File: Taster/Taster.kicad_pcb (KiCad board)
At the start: 2 copper layers, 30 x 30 mm, 55 parts, among them J1 I2C, J2 JTAG, J3 INTERFACE, M1 KNX_KLEMME, SW1 SW_Push, U1 EFM32PG12B500, U2 NCN5120, U3 MX25R8035F, Y1 32.768kHz, Y2 38.4MHz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

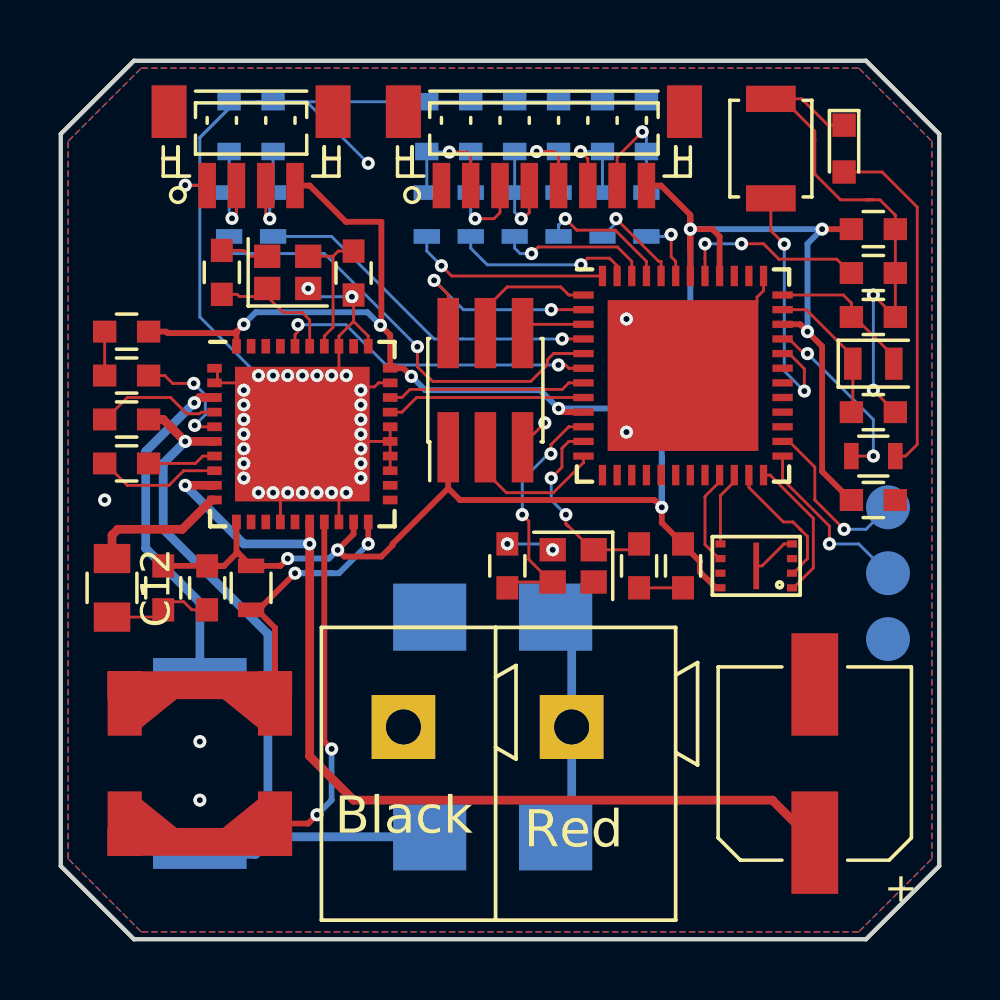
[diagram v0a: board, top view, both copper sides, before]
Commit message: Version 1.1.0 of the Taster board.
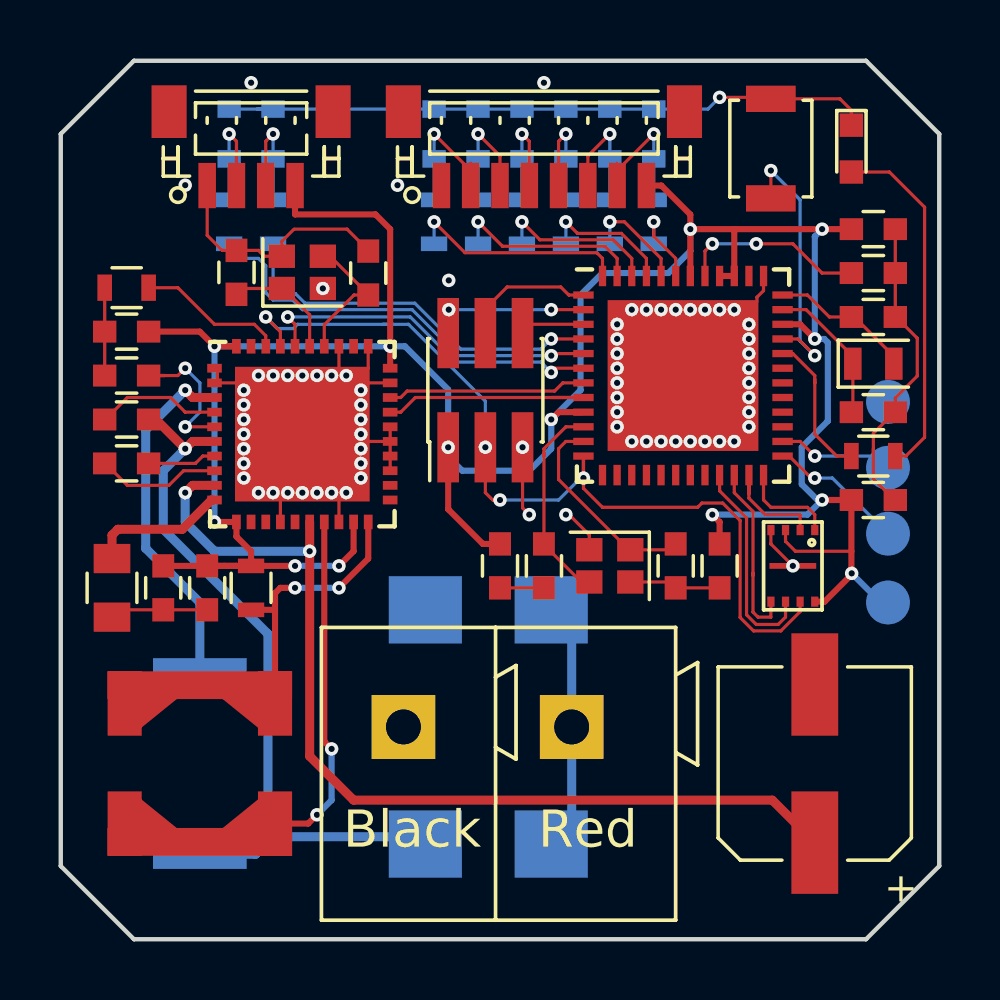
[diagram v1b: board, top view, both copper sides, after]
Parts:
- removed M1: KNX_KLEMME, KNXTransceiverBoard_V1.2:KNXTransceiverBoard_V1.2-KNX_KLEMME
- added C20: 100nF, Capacitors_SMD:C_0603, F.Cu at (85.0, 57.2)
- added J3: KNX_KLEMME, KNX:KNX_KLEMME, F.Cu at (84.2, 62.8)
- added R13: 0, Resistors_SMD:R_0603, F.Cu at (72.2, 47.8)
- added TP4: Test_Point, Measurement_Points:Measurement_Point_Round-SMD-Pad_Small, B.Cu at (98.2, 58.5)
- C14: value 4.7nF -> 220nF
- R2: value 22 -> 27
- SW1: value SW_Push -> PROG
- U2: value NCN5120 -> NCN5121
- moved TP1 5.85 mm to (98.2, 51.6)
- moved TP3 3.60 mm to (98.2, 56.1)
- moved TP2 1.35 mm to (98.2, 53.9)
- moved C10 1.25 mm to (92.5, 57.2)
- moved C4 1.25 mm to (91.0, 57.2)
- moved C5 1.25 mm to (86.5, 57.2), turned to 270 degrees
- moved U3 1.25 mm to (95.0, 57.2), turned to 270 degrees
- moved Y2 1.25 mm to (88.8, 57.2)
- moved C6 0.50 mm to (80.5, 47.2), turned to 90 degrees
- moved C7 0.50 mm to (76.0, 47.2)
- moved Y3 0.50 mm to (78.2, 47.2)
- moved D10 0.35 mm to (84.2, 42.5)
- moved D11 0.35 mm to (82.8, 42.5)
- moved D6 0.35 mm to (90.2, 42.5)
- moved D7 0.35 mm to (88.8, 42.5)
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- renumbered J3 to J2, J2 to J4
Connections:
- C10 pad 1: +3V3 -> 3V3-A
- C16 pad 1: +3V3 -> 3V3-A
- C17 pad 1: +3V3 -> 3V3-A
- C18 pad 1: +3V3 -> 3V3-A
- C8 pad 1: +3V3 -> 3V3-A
- C9 pad 1: +3V3 -> 3V3-A
- J1 pad 4: +3V3 -> 3V3-A
- J2 pad 8: +3V3 -> 3V3-A
- J4 pad 1: +3V3 -> 3V3-A
- R3 pad 1: +3V3 -> 3V3-A
- TP1 pad 1: Net-(TP1-Pad1) -> GND
- TP3 pad 1: GND -> Net-(TP3-Pad1)
- U1 pad 25: Net-(TP1-Pad1) -> Net-(TP3-Pad1)
- U1 pad 32: /SWITCH -> /LED
- U1 pad 33: /LED -> /SWITCH
- U1 pad 34: +3V3 -> 3V3-A
- U1 pad 39: Net-(U1-Pad39) -> 3V3-A
- U1 pad 40: +3V3 -> 3V3-A
- U1 pad 42: +3V3 -> 3V3-A
- U1 pad 9: +3V3 -> 3V3-A
- U2 pad 11: +3V3 -> 3V3-A
- U2 pad 19: +3V3 -> 3V3-A
- U2 pad 30: +3V3 -> 3V3-A
- U2 pad 37: /RESETB -> /RESET
- U2 pad 38: /FANIN -> Net-(R13-Pad2)
- U2 pad 40: +3V3 -> 3V3-A
- U3 pad 3: Net-(U3-Pad3) -> 3V3-A
- U3 pad 7: Net-(U3-Pad7) -> /RESET
- U3 pad 8: +3V3 -> 3V3-A
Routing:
- net 3V3-A: track 0.00 -> 99.1 mm, vias 0 -> 13
- net +3V3: track 93.5 -> 0.00 mm, vias 10 -> 0
- net /RESET: track 5.13 -> 31.9 mm, vias 0 -> 4
- net GND: track 122.4 -> 113.5 mm, vias 42 -> 71
- net Net-(TP1-Pad1): track 6.08 -> 0.00 mm, vias 1 -> 0
- net Net-(R13-Pad2): track 0.00 -> 5.04 mm
- net Net-(TP3-Pad1): track 0.00 -> 4.70 mm, vias 0 -> 1
- net /SCLK: track 3.31 -> 7.25 mm
- net /MOSI: track 2.55 -> 6.23 mm
- net /SWDIO: track 7.51 -> 4.60 mm
- net /SCL: track 16.3 -> 14.5 mm
- net /CS: track 5.02 -> 3.33 mm
- net Net-(TP2-Pad1): track 5.81 -> 4.20 mm
- net Net-(C5-Pad1): track 8.60 -> 7.17 mm, vias 2 -> 0
- net Net-(D11-Pad1): track 3.97 -> 5.31 mm
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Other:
- net class Default: clearance 0.1 -> 0.11; trace_width 0.1 -> 0.11; via_dia 0.45 -> 0.46; via_drill 0.2 -> 0.21
- net class Power: clearance 0.1 -> 0.11; trace_width 0.3 -> 0.31; via_dia 0.45 -> 0.46; via_drill 0.2 -> 0.21
- net class Power-3V3: clearance 0.1 -> 0.11; trace_width 0.2 -> 0.21; via_dia 0.45 -> 0.46; via_drill 0.2 -> 0.21
- rule trace_clearance: 0.1 -> 0.11
- board text added: "BasilFX 06 2018 V1.1.0"
- board text removed: "BasilFX 06/2018 V1.1.0"

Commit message: Version 1.2.0 of board
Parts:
- removed C20: 100nF, Capacitors_SMD:C_0603
- added C19: 100nF, Capacitor_SMD:C_0603_1608Metric, F.Cu at (85.0, 57.2)
- added R12: 0, Resistor_SMD:R_0603_1608Metric, F.Cu at (72.2, 46.5)
- C1, C10, C13, C14, C15, C16, C17, C18, C2, C3, C4, C5, C6, C7, C8, C9: footprint Capacitors_SMD:C_0603 -> Capacitor_SMD:C_0603_1608Metric
- C11: footprint Capacitors_SMD:CP_Elec_6.3x7.7 -> Capacitor_SMD:CP_Elec_6.3x7.7
- C12: footprint Capacitors_SMD:C_0805 -> Capacitor_SMD:C_0805_2012Metric
- D1: footprint LEDs:LED_0603 -> LED_SMD:LED_0603_1608Metric
- D10, D11, D4, D5, D6, D7, D8, D9: footprint Diodes_SMD:D_0603 -> Diode_SMD:D_0603_1608Metric
- D2, D3: footprint Diodes_SMD:D_SMB -> Diode_SMD:D_SMB
- J1: footprint Connectors_JST:JST_SH_BM04B-SRSS-TB_04x1.00mm_Straight -> Connector_JST:JST_SH_BM04B-SRSS-TB_1x04-1MP_P1.00mm_Vertical
- J2: footprint Connectors_JST:JST_SH_BM08B-SRSS-TB_08x1.00mm_Straight -> Connector_JST:JST_SH_BM08B-SRSS-TB_1x08-1MP_P1.00mm_Vertical
- J4: footprint Pin_Headers:Pin_Header_Straight_2x03_Pitch1.27mm_SMD -> Connector_PinHeader_1.27mm:PinHeader_2x03_P1.27mm_Vertical_SMD
- R1, R4, R5, R6, R7, R8, R9: value 220 -> 680; footprint Resistors_SMD:R_0603 -> Resistor_SMD:R_0603_1608Metric
- R10, R11: value 220 -> 0; footprint Resistors_SMD:R_0603 -> Resistor_SMD:R_0603_1608Metric
- R13: footprint Resistors_SMD:R_0603 -> Resistor_SMD:R_0603_1608Metric
- R2: footprint Resistors_SMD:R_2512 -> Resistor_SMD:R_2512_6332Metric
- R3: value R -> 1; footprint Resistors_SMD:R_0603 -> Resistor_SMD:R_0603_1608Metric
- SW1: footprint Buttons_Switches_SMD:SW_SPST_B3U-1000P -> Button_Switch_SMD:SW_SPST_B3U-1000P
- TP1, TP2, TP3, TP4: footprint Measurement_Points:Measurement_Point_Round-SMD-Pad_Small -> TestPoint:TestPoint_Pad_D1.0mm
- U1: footprint Housings_DFN_QFN:QFN-48-1EP_7x7mm_Pitch0.5mm -> Package_DFN_QFN:Infineon_MLPQ-48-1EP_7x7mm_P0.5mm_Pad5.15x5.15mm
- U2: footprint Housings_DFN_QFN:QFN-40-1EP_6x6mm_Pitch0.5mm -> Package_DFN_QFN:QFN-40-1EP_6x6mm_P0.5mm_EP4.6x4.6mm
- Y1: footprint Crystals:Crystal_SMD_2012-2pin_2.0x1.2mm -> Crystal:Crystal_SMD_2012-2Pin_2.0x1.2mm
- Y2: value 38.4MHz -> 40MHz; footprint Crystals:Crystal_SMD_2016-4pin_2.0x1.6mm -> Crystal:Crystal_SMD_2016-4Pin_2.0x1.6mm
- Y3: footprint Crystals:Crystal_SMD_2016-4pin_2.0x1.6mm -> Crystal:Crystal_SMD_2016-4Pin_2.0x1.6mm
- moved TP1 0.27 mm to (98.0, 51.8), turned to 0 degrees
- moved TP2 0.27 mm to (98.0, 54.0), turned to 0 degrees
- moved TP3 0.27 mm to (98.0, 56.2)
- moved C13 0.25 mm to (72.2, 51.0)
- moved C14 0.25 mm to (72.2, 54.0)
- moved C15 0.25 mm to (72.2, 52.5)
- moved C18 0.25 mm to (72.2, 49.5)
- moved R13 0.25 mm to (72.2, 48.0)
- moved TP4 0.25 mm to (98.0, 58.5)
- turned L1 to 90 degrees
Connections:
- U2 pad 37: /RESET -> Net-(R12-Pad2)
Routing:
- net GND: track 113.5 -> 137.9 mm
- net Net-(R12-Pad2): track 0.00 -> 6.69 mm, vias 0 -> 2
- net Net-(L1-Pad2): track 17.7 -> 11.4 mm
- net /RESET: track 31.9 -> 35.0 mm
- net Net-(C11-Pad1): track 33.2 -> 34.3 mm
- net /KNX+: track 26.9 -> 27.8 mm
- net Net-(C13-Pad1): track 5.32 -> 4.48 mm
- net Net-(R2-Pad2): track 12.1 -> 12.9 mm
- net Net-(D6-Pad1): track 5.29 -> 4.53 mm
- net Net-(D11-Pad1): track 5.31 -> 4.55 mm
- net 3V3-A: track 99.1 -> 98.5 mm
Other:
- net class KNX added: clearance 0.19, trace_width 0.31, via_dia 0.46, via_drill 0.21
- net class Power: clearance 0.11 -> 0.19
- board text added: "BasilFX 08/2018 V1.2.0"
- board text removed: "BasilFX 06 2018 V1.1.0"
